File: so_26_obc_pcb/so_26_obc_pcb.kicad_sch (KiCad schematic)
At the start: 0 parts

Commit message: schematic: updated title block
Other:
- company: (none) -> Regine Angermo Birkely
- title: (none) -> so_26_obc_pcb
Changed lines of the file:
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@@
 	(generator_version "9.0")
 	(paper "A4")
+	(title_block
+		(title "so_26_obc_pcb")
+		(date "2026-01-28")
+		(rev "1")
+		(company "Regine Angermo Birkely")
+	)
 	(sheet_instances
 		(path "/"

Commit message: Schematic: Added symbols + MCU setup
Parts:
- added C1, C3, C4, C5, C6, C8: 100n, symbol Device:C_Small
- added C2, C7: 4u7, symbol Device:C_Small
- added SW1: SW_Push, symbol Switch:SW_Push
- added U1: ~, so_26_obc_footprint_library:TSSOP-8_3x3mm_P0.65mm, symbol Temp_symbol_library:PCT2075
- added U2: STM32G431RBTx, Package_QFP:LQFP-64_10x10mm_P0.5mm, symbol MCU_ST_STM32G4:STM32G431RBTx
- added U3: MPRLS0025, symbol so_26_obc_library: MPRLS0025PA00002A
- added U4: LSM6DS3, symbol so_26_obc_library:LSM6DS3TR
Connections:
- new net: C6.1, C7.1, U2.28 (VREF+)
- new net +3V3: C1.1, C2.1, C3.1, C4.1, C5.1, U2.16 (VDD), U2.29 (VDDA), U2.32 (VDD), U2.48 (VDD), U2.64 (VDD)
- new net DEBUG_LED_0: U2.24 (PB0)
- new net GND: C1.2, C2.2, C3.2, C4.2, C5.2, C6.2, C7.2, C8.2, SW1.2, U2.15 (VSS), U2.27 (VSSA), U2.31 (VSS), U2.47 (VSS), U2.63 (VSS)
- new net NRST: C8.1, SW1.1, U2.7 (NRST)
- new net PWM_HEATER: U2.39 (PC7)
- new net RADIO_UART_RX: U2.23 (PC5)
- new net RADIO_UART_TX: U2.22 (PC4)
- new net SD_MISO: U2.59 (PB6)
- new net SD_MOSI: U2.21 (PA7)
- no-connect marks 0 -> 36

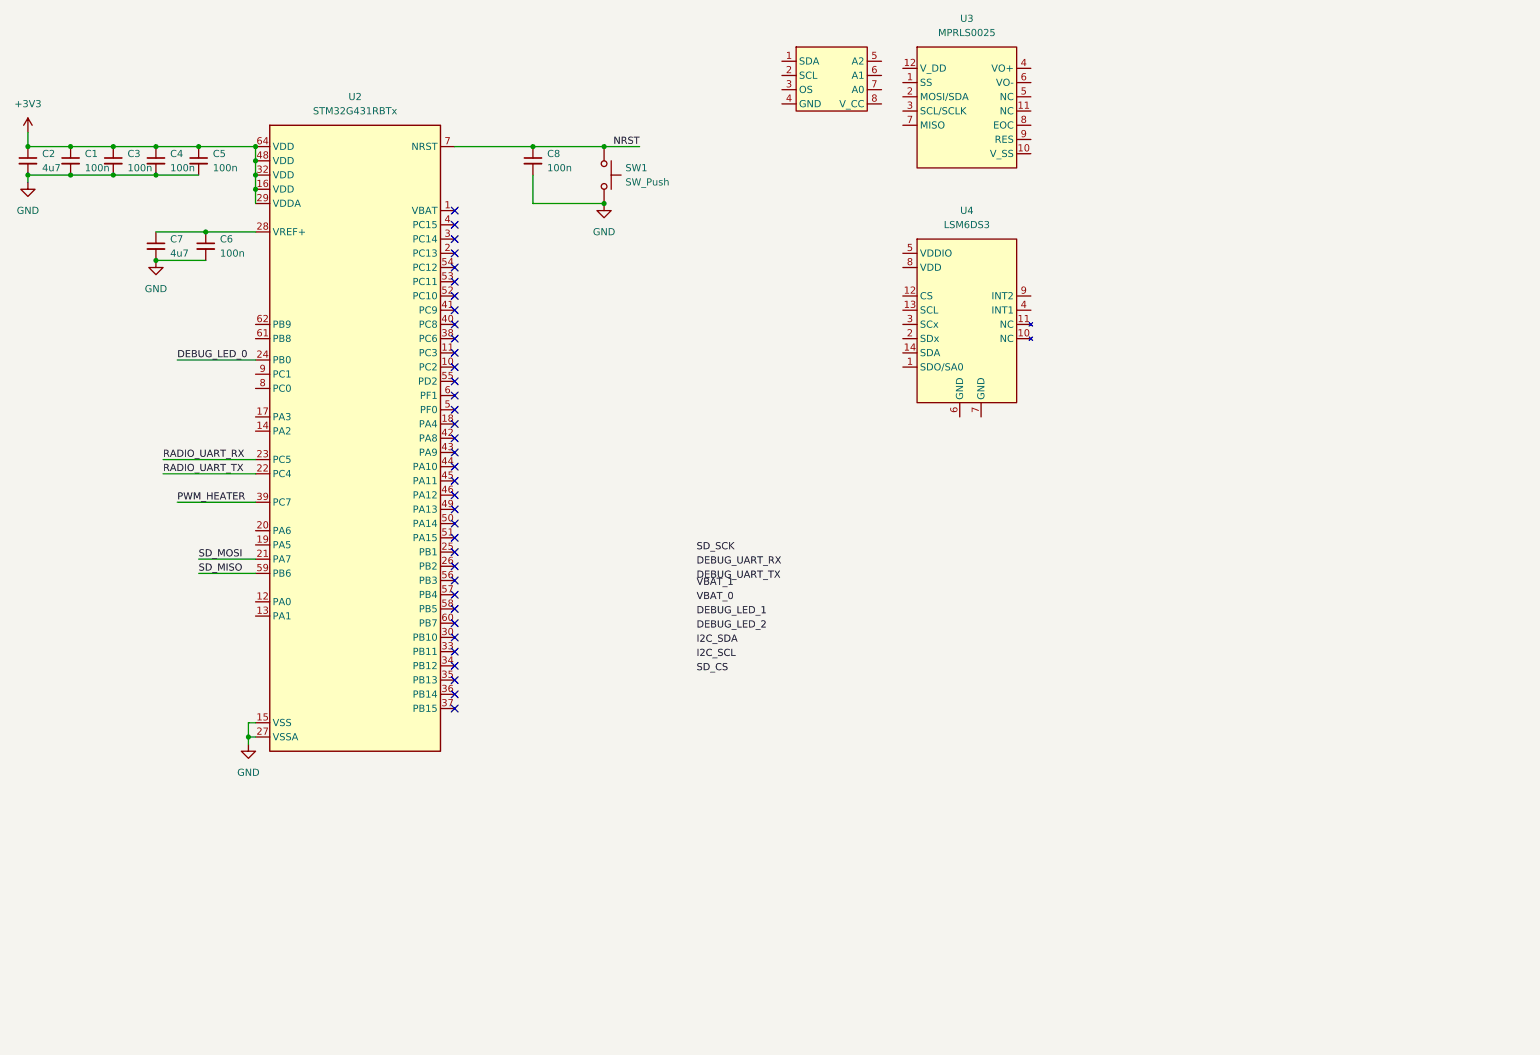
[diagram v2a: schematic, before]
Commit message: schematic: added a lot, every ic basically
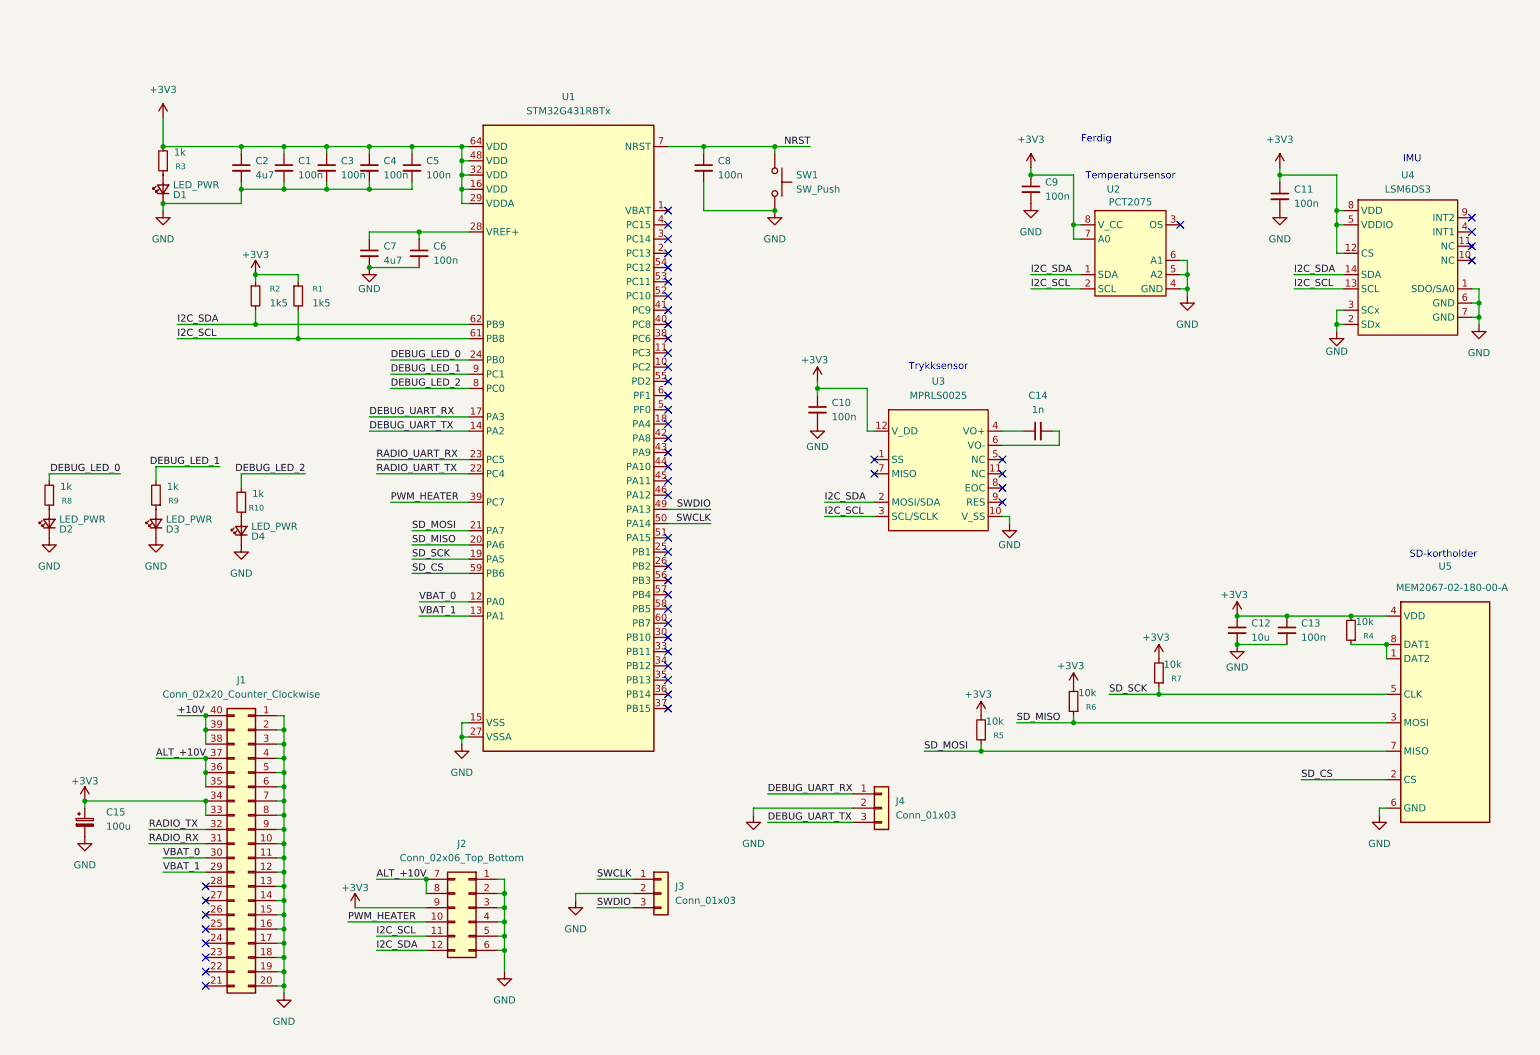
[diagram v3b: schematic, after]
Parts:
- added C10, C11, C13, C9: 100n, symbol Device:C_Small
- added C12: 10u, symbol Device:C_Small
- added C14: 1n, symbol Device:C_Small
- added C15: 100u, symbol Device:C_Polarized_Small
- added D1, D2, D3, D4: LED_PWR, symbol Device:LED_Small
- added J1: Conn_02x20_Counter_Clockwise, symbol Connector_Generic:Conn_02x20_Counter_Clockwise
- added J2: Conn_02x06_Top_Bottom, symbol Connector_Generic:Conn_02x06_Top_Bottom
- added J3, J4: Conn_01x03, symbol Connector_Generic:Conn_01x03
- added R1, R2: 1k5, symbol Device:R_Small
- added R10, R3, R8, R9: 1k, symbol Device:R_Small
- added R4, R5, R6, R7: 10k, symbol Device:R_Small
- added U5: MEM2067-02-180-00-A, so_26_obc_footprint_library:MEM2067-02-180-00-A, symbol so_26_obc_library:MEM2067-02-180-00-A
- U2: renamed from U1; value ~ -> PCT2075
- U3: footprint (none) -> so_26_obc_footprint_library:MPRLS0025PA00002A
- U4: footprint (none) -> so_26_obc_footprint_library:LGA-14_3x2.5mm_P0.5mm_LayoutBorder3x4y
- renumbered U2 to U1
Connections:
- net +3V3: now also U2.7 (A0), U2.8 (V_CC), U3.12 (V_DD), U4.12 (CS), U4.5 (VDDIO), U4.8 (VDD), C10.1, C11.1, C12.1, C13.1, C15.1, C9.1, J1.33 (Pin_33), J1.34 (Pin_34), J2.9 (Pin_9), R1.1, R2.1, R3.2, R4.2, R5.2, R6.2, R7.2, U5.4 (VDD)
- net DEBUG_LED_0: now also R8.2
- net DEBUG_LED_1: now also U1.9 (PC1), R9.2
- net DEBUG_LED_2: now also U1.8 (PC0), R10.2
- net DEBUG_UART_RX: now also U1.17 (PA3), J4.1 (Pin_1)
- net DEBUG_UART_TX: now also U1.14 (PA2), J4.3 (Pin_3)
- net GND: now also U2.4 (GND), U2.5 (A2), U2.6 (A1), U3.10 (V_SS), U4.1 (SDO/SA0), U4.2 (SDx), U4.3 (SCx), U4.6 (GND), U4.7 (GND), C10.2, C11.2, C12.2, C13.2, C15.2, C9.2, D1.1 (K), D2.1 (K), D3.1 (K), D4.1 (K), J1.1 (Pin_1), J1.10 (Pin_10), J1.11 (Pin_11), J1.12 (Pin_12), J1.13 (Pin_13), J1.14 (Pin_14), J1.15 (Pin_15), J1.16 (Pin_16), J1.17 (Pin_17), J1.18 (Pin_18), J1.19 (Pin_19), J1.2 (Pin_2), J1.20 (Pin_20), J1.3 (Pin_3), J1.4 (Pin_4), J1.5 (Pin_5), J1.6 (Pin_6), J1.7 (Pin_7), J1.8 (Pin_8), J1.9 (Pin_9), J2.1 (Pin_1), J2.2 (Pin_2), J2.3 (Pin_3), J2.4 (Pin_4), J2.5 (Pin_5), J2.6 (Pin_6), J3.2 (Pin_2), J4.2 (Pin_2), U5.6 (GND)
- net I2C_SCL: now also U1.61 (PB8), U2.2 (SCL), U3.3 (SCL/SCLK), U4.13 (SCL), J2.11 (Pin_11), R1.2
- net I2C_SDA: now also U1.62 (PB9), U2.1 (SDA), U3.2 (MOSI/SDA), U4.14 (SDA), J2.12 (Pin_12), R2.2
- net PWM_HEATER: now also J2.10 (Pin_10)
- net SD_CS: now also U1.59 (PB6), U5.2 (CS)
- net SD_MISO: now also U1.20 (PA6), R6.1, U5.3 (MOSI); no longer U1.59 (PB6)
- net SD_MOSI: now also R5.1, U5.7 (MISO)
- net SD_SCK: now also U1.19 (PA5), R7.1, U5.5 (CLK)
- net VBAT_0: now also U1.12 (PA0), J1.30 (Pin_30)
- net VBAT_1: now also U1.13 (PA1), J1.29 (Pin_29)
- net SWDIO: now reaches U1.49 (PA13)
- net SWDIO: now also J3.3 (Pin_3)
- net SWCLK: now reaches U1.50 (PA14)
- net SWCLK: now also J3.1 (Pin_1)
- net at U3.4 (VO+): now also C14.1
- net at U3.6 (VO-): now also C14.2
- new net: D1.2 (A), R3.1
- new net: D2.2 (A), R8.1
- new net: R4.1, U5.1 (DAT2), U5.8 (DAT1)
- new net: D4.2 (A), R10.1
- new net: D3.2 (A), R9.1
- new net +10V: J1.38 (Pin_38), J1.39 (Pin_39), J1.40 (Pin_40)
- new net ALT_+10V: J1.35 (Pin_35), J1.36 (Pin_36), J1.37 (Pin_37), J2.7 (Pin_7), J2.8 (Pin_8)
- new net RADIO_RX: J1.31 (Pin_31)
- new net RADIO_TX: J1.32 (Pin_32)
- no-connect marks 36 -> 53
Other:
- note added: "Ferdig"
- note added: "IMU"
- note added: "SD-kortholder"
- note added: "Temperatursensor"
- note added: "Trykksensor"
- moved on the sheet: C1, C2, C3, C4, C5, C6, C7, C8, SW1, U1, U3, U4

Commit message: checked by aj
schematic
- fixed mistakes

pcb
- added shape and stack
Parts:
- removed J1: Conn_02x20_Counter_Clockwise, symbol Connector_Generic:Conn_02x20_Counter_Clockwise
- removed J2: Conn_02x06_Top_Bottom, symbol Connector_Generic:Conn_02x06_Top_Bottom
- removed J3: Conn_01x03, symbol Connector_Generic:Conn_01x03
- added C8: 100n, Capacitor_SMD:C_0805_2012Metric_Pad1.18x1.45mm_HandSolder, symbol Device:C_Small
- added J1: Conn_02x12_Odd_Even, Connector_PinSocket_2.54mm:PinSocket_2x12_P2.54mm_Vertical, symbol Connector_Generic:Conn_02x12_Odd_Even
- added J2: Conn_02x06_Odd_Even, Connector_PinSocket_2.54mm:PinSocket_2x06_P2.54mm_Vertical, symbol Connector_Generic:Conn_02x06_Odd_Even
- added J3: Conn_01x04, Connector_PinHeader_2.54mm:PinHeader_1x04_P2.54mm_Vertical, symbol Connector_Generic:Conn_01x04
- added J5: Conn_01x03, Connector_PinHeader_2.54mm:PinHeader_1x03_P2.54mm_Vertical, symbol Connector_Generic:Conn_01x03
- C1: renamed from C15; footprint (none) -> Capacitor_THT:CP_Radial_D6.3mm_P2.50mm
- C10: renamed from C8; footprint (none) -> Capacitor_SMD:C_0805_2012Metric_Pad1.18x1.45mm_HandSolder
- C11: renamed from C10; footprint (none) -> Capacitor_SMD:C_0805_2012Metric_Pad1.18x1.45mm_HandSolder
- C12: renamed from C9; footprint (none) -> Capacitor_SMD:C_0805_2012Metric_Pad1.18x1.45mm_HandSolder
- C13: renamed from C14; footprint (none) -> Capacitor_SMD:C_0805_2012Metric_Pad1.18x1.45mm_HandSolder
- C14: renamed from C12; footprint (none) -> Capacitor_SMD:C_1206_3216Metric_Pad1.33x1.80mm_HandSolder
- C15: renamed from C11; footprint (none) -> Capacitor_SMD:C_0805_2012Metric_Pad1.18x1.45mm_HandSolder
- C16: renamed from C13; footprint (none) -> Capacitor_SMD:C_0805_2012Metric_Pad1.18x1.45mm_HandSolder
- C2, C7: footprint (none) -> Capacitor_SMD:C_1206_3216Metric_Pad1.33x1.80mm_HandSolder
- C3: renamed from C1; footprint (none) -> Capacitor_SMD:C_0805_2012Metric_Pad1.18x1.45mm_HandSolder
- C4: renamed from C3; footprint (none) -> Capacitor_SMD:C_0805_2012Metric_Pad1.18x1.45mm_HandSolder
- C5: renamed from C4; footprint (none) -> Capacitor_SMD:C_0805_2012Metric_Pad1.18x1.45mm_HandSolder
- C6: renamed from C5; footprint (none) -> Capacitor_SMD:C_0805_2012Metric_Pad1.18x1.45mm_HandSolder
- C9: renamed from C6; footprint (none) -> Capacitor_SMD:C_0805_2012Metric_Pad1.18x1.45mm_HandSolder
- D1: renamed from D2; value LED_PWR -> BLUE; footprint (none) -> LED_SMD:LED_0805_2012Metric_Pad1.15x1.40mm_HandSolder
- D2: renamed from D1; footprint (none) -> LED_SMD:LED_0805_2012Metric_Pad1.15x1.40mm_HandSolder
- D3: value LED_PWR -> YELLOW; footprint (none) -> LED_SMD:LED_0805_2012Metric_Pad1.15x1.40mm_HandSolder
- D4: value LED_PWR -> GREEN; footprint (none) -> LED_SMD:LED_0805_2012Metric_Pad1.15x1.40mm_HandSolder
- J4: footprint (none) -> Connector_PinHeader_2.54mm:PinHeader_1x03_P2.54mm_Vertical
- R1: renamed from R8; value 1k -> 10k; footprint (none) -> Resistor_SMD:R_0805_2012Metric_Pad1.20x1.40mm_HandSolder
- R10: renamed from R4; footprint (none) -> Resistor_SMD:R_0805_2012Metric_Pad1.20x1.40mm_HandSolder
- R2: renamed from R3; value 1k -> 10k; footprint (none) -> Resistor_SMD:R_0805_2012Metric_Pad1.20x1.40mm_HandSolder
- R3: renamed from R9; value 1k -> 10k; footprint (none) -> Resistor_SMD:R_0805_2012Metric_Pad1.20x1.40mm_HandSolder
- R4: renamed from R10; value 1k -> 10k; footprint (none) -> Resistor_SMD:R_0805_2012Metric_Pad1.20x1.40mm_HandSolder
- R5: renamed from R2; footprint (none) -> Resistor_SMD:R_0805_2012Metric_Pad1.20x1.40mm_HandSolder
- R6: renamed from R1; footprint (none) -> Resistor_SMD:R_0805_2012Metric_Pad1.20x1.40mm_HandSolder
- R7: renamed from R5; footprint (none) -> Resistor_SMD:R_0805_2012Metric_Pad1.20x1.40mm_HandSolder
- R8: renamed from R6; footprint (none) -> Resistor_SMD:R_0805_2012Metric_Pad1.20x1.40mm_HandSolder
- R9: renamed from R7; footprint (none) -> Resistor_SMD:R_0805_2012Metric_Pad1.20x1.40mm_HandSolder
- SW1: footprint (none) -> Button_Switch_THT:SW_PUSH_6mm
- U3: renamed from U2; footprint so_26_obc_footprint_library:TSSOP-8_3x3mm_P0.65mm -> Package_SO:TSSOP-8_3x3mm_P0.65mm
- U4: footprint so_26_obc_footprint_library:LGA-14_3x2.5mm_P0.5mm_LayoutBorder3x4y -> Package_LGA:LGA-14_3x2.5mm_P0.5mm_LayoutBorder3x4y
- renumbered U3 to U2
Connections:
- net RADIO_UART_RX is gone; now on net RADIO_RX: U1.23 (PC5)
- net RADIO_UART_TX is gone; now on net RADIO_TX: U1.22 (PC4)
- net +10V: now also J1.2 (Pin_2), J1.4 (Pin_4), J1.6 (Pin_6)
- net +3V3: now also C8.1, J1.14 (Pin_14), J1.16 (Pin_16), J2.6 (Pin_6), J5.1 (Pin_1)
- net ALT_+10V: now also J1.10 (Pin_10), J1.12 (Pin_12), J1.8 (Pin_8), J2.2 (Pin_2)
- net GND: now also C8.2, J1.1 (Pin_1), J1.11 (Pin_11), J1.13 (Pin_13), J1.15 (Pin_15), J1.17 (Pin_17), J1.19 (Pin_19), J1.21 (Pin_21), J1.23 (Pin_23), J1.3 (Pin_3), J1.5 (Pin_5), J1.7 (Pin_7), J1.9 (Pin_9), J2.1 (Pin_1), J2.11 (Pin_11), J2.3 (Pin_3), J2.5 (Pin_5), J2.7 (Pin_7), J2.9 (Pin_9), J3.2 (Pin_2), J5.3 (Pin_3)
- net I2C_SDA: now also J2.12 (Pin_12)
- net NRST: now also J3.4 (Pin_4)
- net PWM_HEATER: now also J2.8 (Pin_8)
- net RADIO_RX: now also J1.20 (Pin_20)
- net RADIO_TX: now also J1.18 (Pin_18)
- net SD_MISO: now also R7.1, U5.7 (MISO); no longer R8.1, U5.3 (MOSI)
- net SD_MOSI: now also R8.1, U5.3 (MOSI); no longer R7.1, U5.7 (MISO)
- net SWCLK: now also J3.1 (Pin_1)
- net SWDIO: now also J3.3 (Pin_3)
- net VBAT_0: now also J1.22 (Pin_22)
- net VBAT_1: now also J1.24 (Pin_24)
- net DEBUG_LED_0 renamed LED_BLUE
- net DEBUG_LED_1 renamed LED_YELLOW
- net DEBUG_LED_2 renamed LED_GREEN
- net I2C_SCL renamed BOOT0
- net BOOT0: now also J2.10 (Pin_10), J5.2 (Pin_2)
- no-connect marks 53 -> 45
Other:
- moved on the sheet: C13, C14, C16, C2, C3, C4, C5, C6, D1, D2, D4, J4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

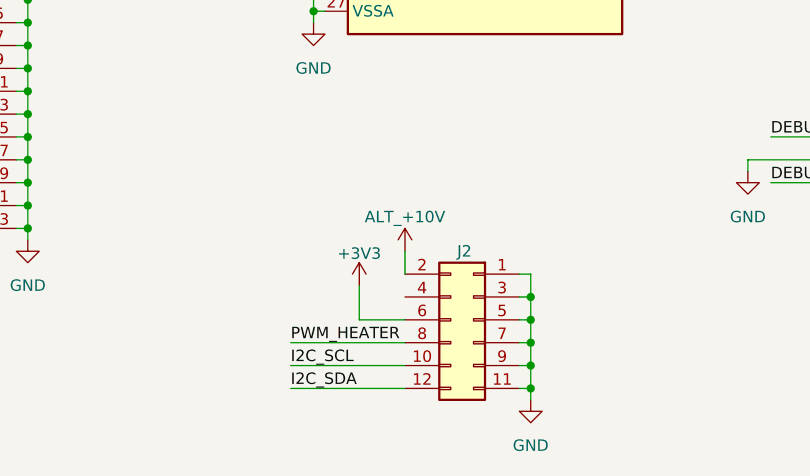
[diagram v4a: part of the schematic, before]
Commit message: checked by aj -> sch: fixed J2 missing connection
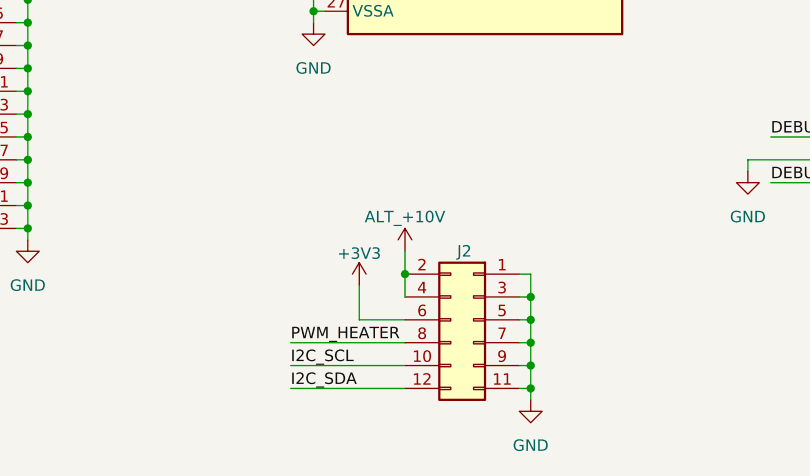
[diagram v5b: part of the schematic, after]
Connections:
- net ALT_+10V: now also J2.4 (Pin_4)
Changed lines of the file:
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@@
+	)
+	(junction
+		(at 101.6 172.72)
+		(diameter 0)
+		(color 0 0 0 0)
 	)
 	(junction
@@
 		)
 		(stroke
+			(width 0)
+			(type default)
+		)
+	)
+	(wire
+		(pts
+			(xy 101.6 172.72) (xy 101.6 175.26)
+		)
+		(stroke
